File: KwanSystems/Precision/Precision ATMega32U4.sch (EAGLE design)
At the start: 151 parts, among them U201 5319, U401 ATMEGA32U4QFN2, Y401 16MHz

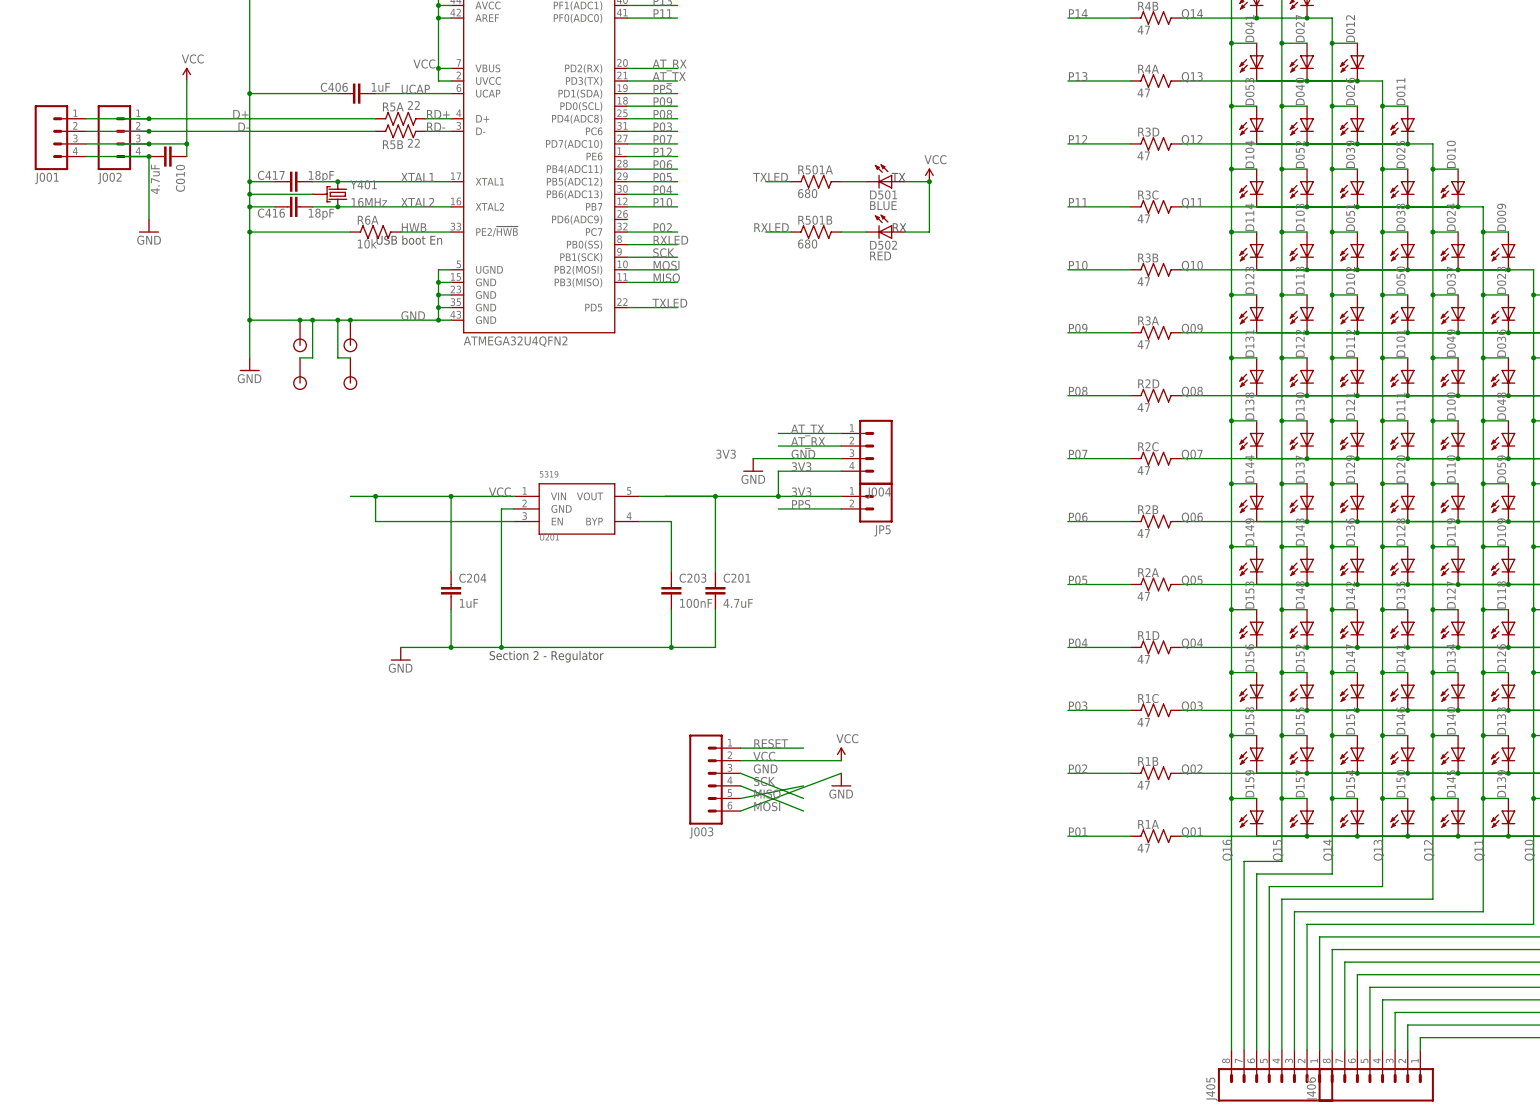
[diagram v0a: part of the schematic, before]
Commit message: Added Yukari4, changed it over to use templates
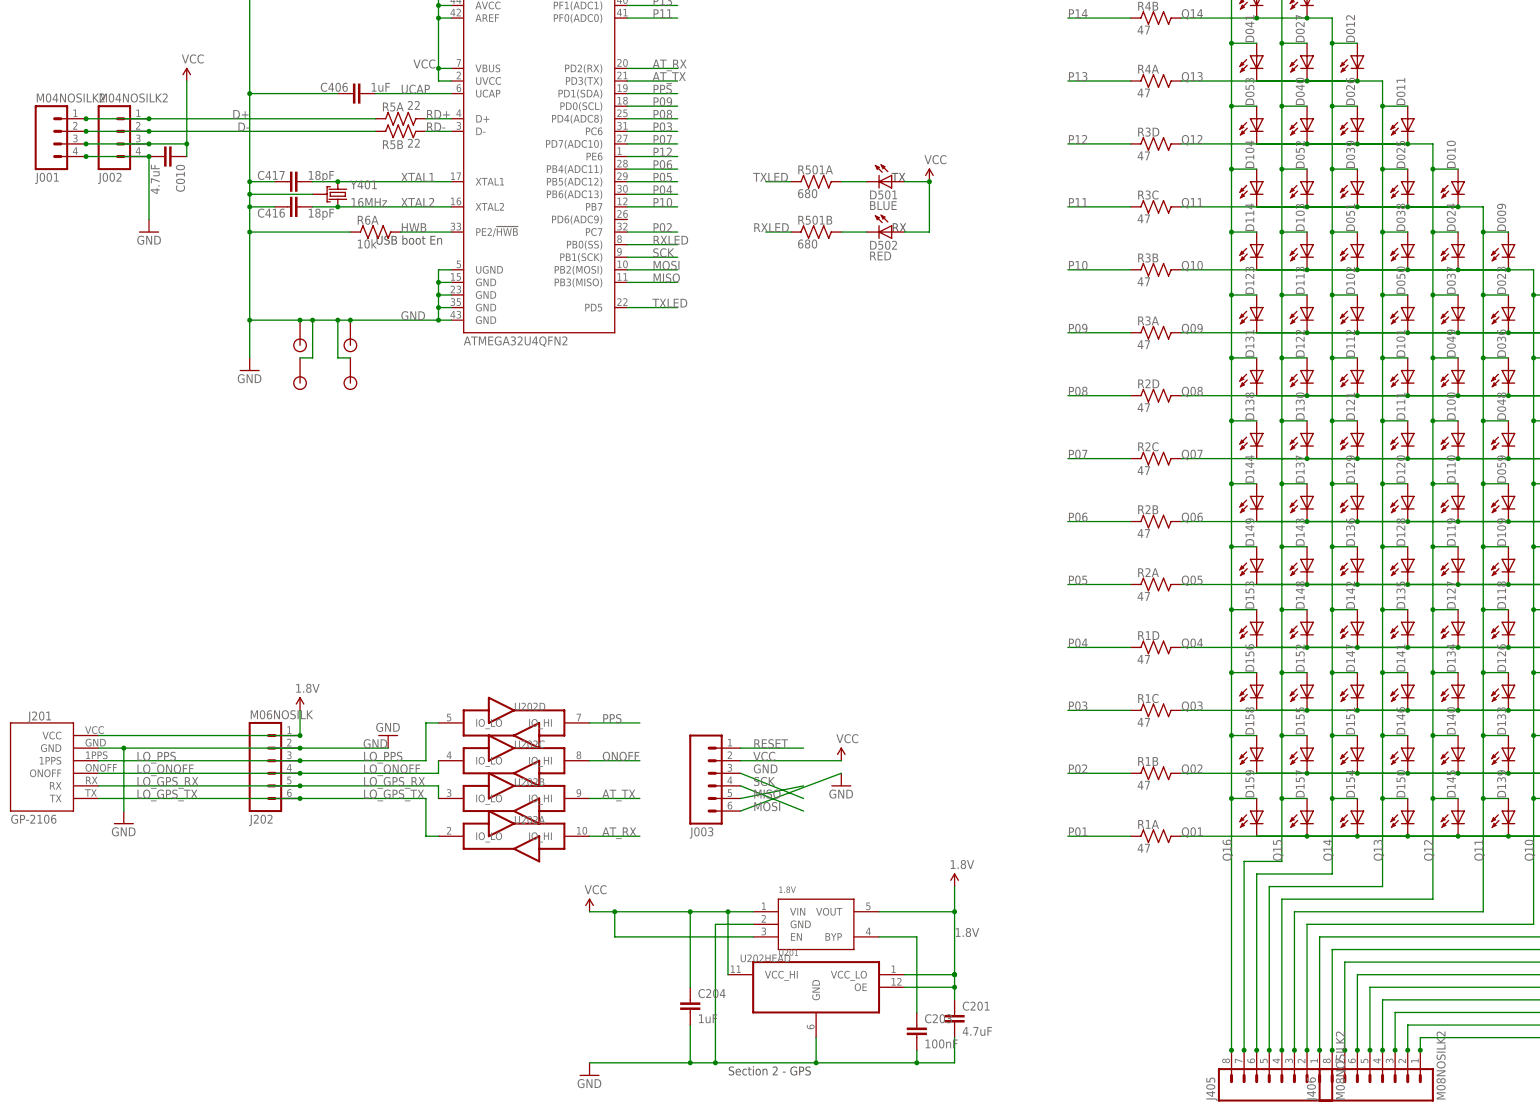
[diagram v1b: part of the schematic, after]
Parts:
- removed J004: (no value), SparkFun:M04PTH
- removed JP5: (no value), SparkFun:M02PTH
- added J201: GP-2106, SparkFun:GP-2106
- added J202: M06NOSILK, KwanSystems:M06NOSILK
- added U202: TXB0104RUT, KwanSystems:TXB0104RUT
- J001, J002: value (none) -> M04NOSILK2; device SparkFun:M04PTH -> KwanSystems:M04NOSILK2
- J405, J406: value (none) -> M08NOSILK2; device SparkFun:M081X08 -> KwanSystems:M08NOSILK2
- U201: value 5319 -> 1.8V
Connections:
- net N$17 renamed BYP
- removed net 3V3: C201.1, J004.4, JP5.1, U201.VOUT
- new net 1.8V: C201.1, J201.VCC, J202.1, U201.VOUT, U202HEAD.OE, U202HEAD.VCC_LO
- new net LO_GPS_RX: J201.RX, J202.5, U202B.IO_LO
- new net LO_GPS_TX: J201.TX, J202.6, U202A.IO_LO
- new net LO_ONOFF: J201.ONOFF, J202.4, U202C.IO_LO
- new net LO_PPS: J201.1PPS, J202.3, U202D.IO_LO
- new net ONOFF: U202C.IO_HI
- net AT_RX: now also U202A.IO_HI; no longer J004.2
- net AT_TX: now also U202B.IO_HI; no longer J004.1
- net GND: now also J201.GND, J202.2, U202HEAD.GND; no longer J004.3
- net PPS: now also U202D.IO_HI; no longer JP5.2
- net VCC: now also U202HEAD.VCC_HI
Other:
- note added: "Section 2 - GPS"
- note removed: "Section 2 - Regulator"
- moved on the sheet: C201, C203, C204, U201
